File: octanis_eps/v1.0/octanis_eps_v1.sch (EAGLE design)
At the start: 141 parts, among them IC1 OPA2333DGK, Q1 32.768kHz, Q100 BSS123, U1 CSD16327Q3_DQG_8, U10 CSD16327Q3_DQG_8, U100 Value, U11 CSD16327Q3_DQG_8, U2 CSD16327Q3_DQG_8, U3 CSD16327Q3_DQG_8, U4 MSP430G2544, U5 TPS2022D, U6 Value, U7 Value, U8 TPS61232, U9 BQ24650_RVA_16

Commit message: restored old v0.5, renamed v1.0 correctly
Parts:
- removed U100: Value, octanis_eps_v05:TPS630250RNCR
- added Q2: BSC340N08NS3G, transistor-power:BSC340N08NS3G
- added R42: dnp, resistor:R-EU_R0603
- added U12: TPS630250YFFT, texasinstruments:TPS630250YFFT
- added U13: (no value), Seeed-OPL-ic:PMIC-CJ78M05(TO-252)
- added U14: CSD16327Q3_DQG_8, texasinstruments:CSD16327Q3_DQG_8
- added U15: MSP430FR5969, chips:MSP430FR5969
- R35: value 270k -> 100k
- U6, U7: value Value -> TPS630250YFFT; device octanis_eps_v05:TPS630250RNCR -> texasinstruments:TPS630250YFFT
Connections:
- removed net N$30: Q1.1, U4.XIN/P2.6
- removed net N$36: Q1.2, U4.XOUT/P2.7
- removed net N$75: JP2.2, U4.TEST/SBWTCK
- removed net N$93: JP2.1, R19.1, U4.RST/NMI/SBWTDIO
- removed net N$99: C3.1, FERRITE.2, U4.AVCC
- new net AGND: C3.2, U15.AVSS
- new net N$10: C3.1, FERRITE.1, U15.AVCC
- new net N$13: JP2.1, R19.1, U15.RST/SBWTDIO
- new net N$15: JP2.2, U15.TEST/SBWTCK
- new net N$16: Q1.1, U15.LFXOUT
- new net N$17: Q1.2, U15.LFXIN
- new net N$9: R42.1, U$1.MODE
- net +3V3: now also FERRITE.2, U12.FB, U12.VOUT, U12.VOUT_2, U12.VOUT_3, U15.DVCC; no longer FERRITE.1, U4.DVCC, U7.FB, U7.VOUT, U7.VOUT_2, U7.VOUT_3
- net +3V3_2: now also U7.FB, U7.VOUT, U7.VOUT_2, U7.VOUT_3; no longer U100.FB, U100.VOUT, U100.VOUT_2, U100.VOUT_3
- net A_EXT1: now also JP1.7, U15.P4.0/A8; no longer JP1.1, U4.P2.4/TA2/A4/VREF+/VEREF+
- net A_EXT2: now also JP1.5, U15.P4.1/A9; no longer JP1.3, U4.P3.0/UCB0STE/UCA0CLK/A5
- net A_EXT3: now also JP1.3, U15.P4.2/A10; no longer JP1.5, U4.P3.6/A6
- net A_EXT4: now also JP1.1, U15.P4.3/A11; no longer JP1.7, U4.P3.7/A7
- net BAT_OUT: now also U12.EN, U12.VIN, U12.VINA, U12.VIN_2, U12.VIN_3; no longer U100.VIN, U100.VINA, U100.VIN_2, U100.VIN_3, U7.EN
- net EN_12V: now also U15.P3.5/TB0.4; no longer U4.P1.7/TA2/TDO/TDI
- net EN_3V3_1: now also U15.P4.5; no longer U4.P1.4/SMCLK/TCK
- net EN_3V3_2: now also U15.P4.6, U7.EN; no longer U100.EN, U4.P1.5/TA0/TMS
- net EN_3V3_M: now also U15.P4.4/TB0.5; no longer U4.P1.3/TA2
- net EN_5V: now also U15.P3.6/TB0.5; no longer U4.P1.6/TA1/TDI
- net EN_SC: now also U15.P3.4/TB0.3; no longer U4.P2.5/ROSC
- net GND: now also R42.2, U12.GND, U12.PFM_PWM, U12.PGND, U12.PGND_2, U12.PGND_3, U15.DVSS, U15.VSS_QFN, U6.PGND_2, U6.PGND_3, U7.PGND_2, U7.PGND_3; no longer C3.2, U100.GND, U100.PFM_PWM, U100.PGND, U4.AVSS, U4.DVSS
- net I2C_SCL: now also U15.P1.7/TB0.4/UCB0SOMI/UCB0SCL/TA1.0; no longer U4.P3.2/UCB0SOMI/UCB0SCL
- net I2C_SDA: now also U15.P1.6/TB0.3/UCB0SIMO/UCB0SDA/TA0.0; no longer U4.P3.1/UCB0SIMO/UCB0SDA
- net I_IN: now also U15.P1.1/TA0.2/A1/C1; no longer U4.P2.1/TAINCLK/SMCLK/A1
- net I_OUT: now also U15.P1.0/TA0.1/A0/C0; no longer U4.P2.0/ACLK/A0
- net N$1: now also U12.L1, U12.L1_2, U12.L1_3; no longer U7.L1
- net N$11: now also U7.L1, U7.L1_2, U7.L1_3; no longer U100.L1
- net N$12: now also U7.L2, U7.L2_2, U7.L2_3; no longer U100.L2
- net N$3: now also U12.L2, U12.L2_2, U12.L2_3; no longer U7.L2
- net N$6: now also U6.L1_2, U6.L1_3
- net N$7: now also U6.L2_2, U6.L2_3
- net V_BAT: now also U15.P1.3/TA1.2/UCB0STE/A3/C3; no longer U4.P2.3/TA1/A3/VREF−/VEREF-
- net V_SC: now also U15.P1.2/TA1.1/A2/C2; no longer U4.P2.2/TA0/A2
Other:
- note added: "-> R_ILIM = 100k --> switch current limit = 11.7 A"
- moved on the sheet: C10, C104, C3, C4, C7, FERRITE, JP2, Q1, R104, R19, R27

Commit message: now all EPS components are on top side
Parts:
- removed JP1: (no value), Headerlibrary:PINHD-2X4
- removed U13: (no value), Seeed-OPL-ic:PMIC-CJ78M05(TO-252)
- removed U14: CSD16327Q3_DQG_8, texasinstruments:CSD16327Q3_DQG_8
- added C39, C40: 12pF, rcl:C-EUC0603
- added JP7: (no value), adafruit:PINHD-1X6B
- added JP8: (no value), Headerlibrary:PINHD-2X6
- added R43: 1M, rcl:R-EU_R0603
- added RT1, RT3, RT4: 2723, rcl:R-EU_R0603
- added RT2: 8501, rcl:R-EU_R0603
- added RTH: (no value), Headerlibrary:PINHD-1X2
- added U$4: MIC4414, Octanis1_EPS:MIC4414
- Q2: value BSC340N08NS3G -> BSC0901NS
- R41: device rcl:R-EU_R2012 -> rcl:R-EU_R2010
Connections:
- new net A4_EXT: JP8.11, RT3.2, U15.P1.4/TB0.1/UCA0STE/A4/C4
- new net A5_EXT: JP8.9, RT4.2, U15.P1.5/TB0.2/UCA0CLK/A5/C5
- new net AVCC: C3.1, FERRITE.1, RT3.1, RT4.1, U15.AVCC
- new net BAT_11V: C33.1, C34.1, C35.1, L4.1, Q2G$1.S, U$1.EN, U$1.VIN
- new net N$18: JP7.3, U15.P2.1/TB0.0/UCA0RXD/UCA0SOMI
- new net N$28: JP7.4, U15.P2.0/TB0.6/UCA0TXD/UCA0SIMO
- new net N$29: JP7.2, U15.P2.3/TA0.0/UCA1STE/A6
- new net N$30: JP7.1, U15.P2.4/TA1.0/UCA1CLK/A7
- new net N$36: JP7.5, U15.P2.6/TB0.1/UCA1RXD/UCA1SOMI
- new net N$41: JP7.6, U15.P2.5/TB0.0/UCA1TXD/UCA1SIMO
- new net TS: RT1.2, RT2.1, RTH.2, U9.TS
- net AGND: now also C39.1, C40.1, JP8.10, JP8.12, JP8.2, JP8.4, JP8.6, JP8.8, Q1.GND
- net A_EXT1: now also JP8.7; no longer JP1.7
- net A_EXT2: now also JP8.5; no longer JP1.5
- net A_EXT3: now also JP8.3; no longer JP1.3
- net A_EXT4: now also JP8.1; no longer JP1.1
- net BAT_OUT: now also Q2G$1.D, U$4.VDD; no longer C33.1, C34.1, C35.1, L4.1, U$1.VIN
- net EN_12V: now also R43.2, U$4.IN; no longer U$1.EN
- net GND: now also R43.1, RT2.2, RTH.1, U$4.GND; no longer JP1.2, JP1.4, JP1.6, JP1.8, Q1.GND
- net N$10: now also Q2G$1.G, U$4.OUT; no longer C3.1, FERRITE.1, U15.AVCC
- net N$16: now also C39.2
- net N$17: now also C40.2
- net N$72: now also RT1.1
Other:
- note added: "The effective load capacitance, CL,eff can be computed as CIN x COUT / (CIN + COUT), where CIN and COUT are the total capacitance at the LFXIN and LFXOUT terminals, respectively. Cin = 2pF Requires external capacitors at both terminals to meet the effective load capacitance specified by crystal manufacturers. Recommended effective load capacitance values supported are 3.7 pF, 6 pF, 9 pF, and 12.5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"
- moved on the sheet: C23, Q2, R41

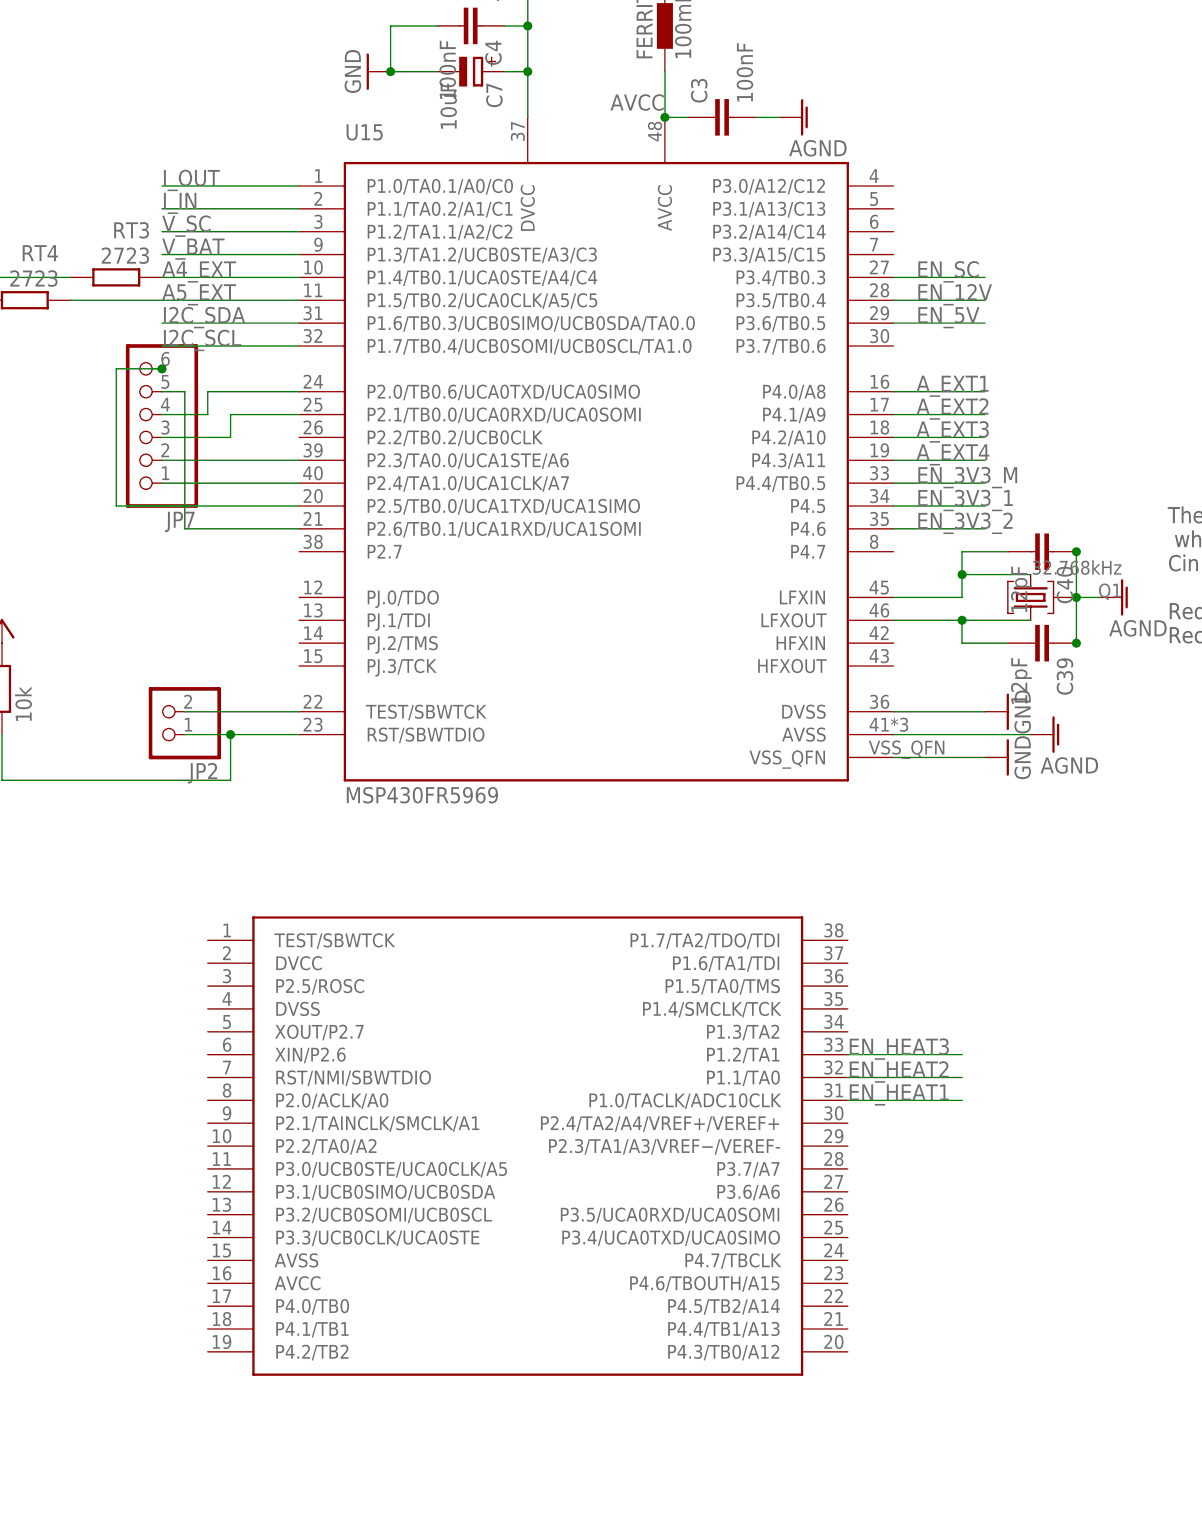
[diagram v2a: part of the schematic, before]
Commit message: finished component placement of new EPS
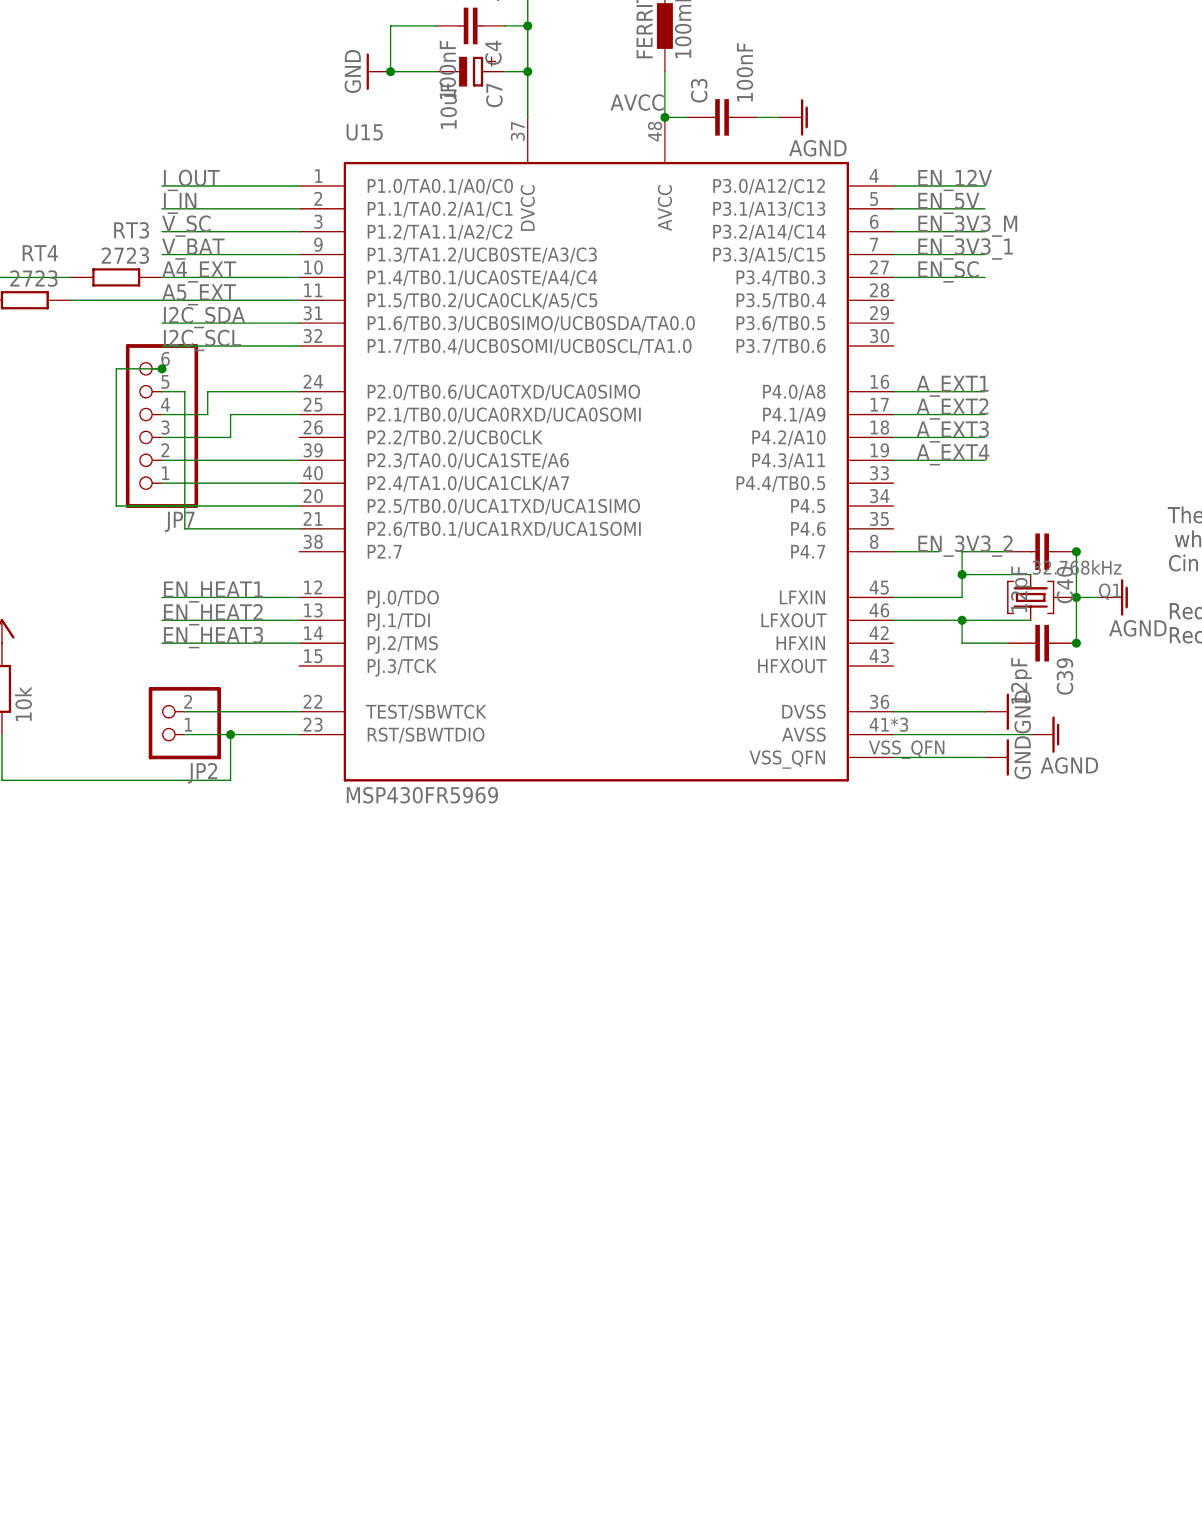
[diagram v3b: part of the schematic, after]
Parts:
- removed U4: MSP430G2544, Octanis1_EPS:MSP430G2544
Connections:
- net EN_12V: now also U15.P3.0/A12/C12; no longer U15.P3.5/TB0.4
- net EN_3V3_1: now also U15.P3.3/A15/C15; no longer U15.P4.5
- net EN_3V3_2: now also U15.P4.7; no longer U15.P4.6
- net EN_3V3_M: now also U15.P3.2/A14/C14; no longer U15.P4.4/TB0.5
- net EN_5V: now also U15.P3.1/A13/C13; no longer U15.P3.6/TB0.5
- net EN_HEAT1: now also U15.PJ.0/TDO; no longer U4.P1.0/TACLK/ADC10CLK
- net EN_HEAT2: now also U15.PJ.1/TDI; no longer U4.P1.1/TA0
- net EN_HEAT3: now also U15.PJ.2/TMS; no longer U4.P1.2/TA1
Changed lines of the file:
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@@
 <part name="U9" library="octanis_eps_v05" deviceset="BQ24650_RVA_16" device=""/>
 <part name="U5" library="Octanis1_EPS" deviceset="TPS2022D" device=""/>
-<part name="U4" library="Octanis1_EPS" deviceset="MSP430G2544" device=""/>
 <part name="C14" library="resistor" deviceset="C-EU" device="C0805" value="10uF"/>
 <part name="C5" library="resistor" deviceset="C-EU" device="C0805" value="22uF"/>
@@
 <instance part="U9" gate="A" x="99.06" y="68.58"/>
 <instance part="U5" gate="G$1" x="419.1" y="175.26"/>
-<instance part="U4" gate="G$1" x="101.6" y="261.62"/>
 <instance part="C14" gate="G$1" x="297.18" y="165.1"/>
 <instance part="C5" gate="G$1" x="365.76" y="165.1"/>
@@
 </segment>
 <segment>
-<pinref part="U4" gate="G$1" pin="P1.0/TACLK/ADC10CLK"/>
-<wire x1="137.16" y1="266.7" x2="149.86" y2="266.7" width="0.1524" layer="91"/>
-<label x="137.16" y="266.7" size="1.778" layer="95"/>
+<pinref part="U15" gate="G$1" pin="PJ.0/TDO"/>
+<wire x1="76.2" y1="322.58" x2="68.58" y2="322.58" width="0.1524" layer="91"/>
+<wire x1="68.58" y1="322.58" x2="60.96" y2="322.58" width="0.1524" layer="91"/>
+<label x="60.96" y="322.58" size="1.778" layer="95"/>
 </segment>
 </net>
@@
 </segment>
 <segment>
-<pinref part="U4" gate="G$1" pin="P1.1/TA0"/>
-<wire x1="137.16" y1="269.24" x2="149.86" y2="269.24" width="0.1524" layer="91"/>
-<label x="137.16" y="269.24" size="1.778" layer="95"/>
+<pinref part="U15" gate="G$1" pin="PJ.1/TDI"/>
+<wire x1="76.2" y1="320.04" x2="60.96" y2="320.04" width="0.1524" layer="91"/>
+<label x="60.96" y="320.04" size="1.778" layer="95"/>
 </segment>
 </net>
@@
 </segment>
 <segment>
-<pinref part="U4" gate="G$1" pin="P1.2/TA1"/>
-<wire x1="137.16" y1="271.78" x2="149.86" y2="271.78" width="0.1524" layer="91"/>
-<label x="137.16" y="271.78" size="1.778" layer="95"/>
+<pinref part="U15" gate="G$1" pin="PJ.2/TMS"/>
+<wire x1="76.2" y1="317.5" x2="60.96" y2="317.5" width="0.1524" layer="91"/>
+<label x="60.96" y="317.5" size="1.778" layer="95"/>
 </segment>
 </net>
@@
 </segment>
 <segment>
-<pinref part="U15" gate="G$1" pin="P4.6"/>
-<wire x1="142.24" y1="330.2" x2="152.4" y2="330.2" width="0.1524" layer="91"/>
-<label x="144.78" y="330.2" size="1.778" layer="95"/>
+<pinref part="U15" gate="G$1" pin="P4.7"/>
+<wire x1="142.24" y1="327.66" x2="147.32" y2="327.66" width="0.1524" layer="91"/>
+<label x="144.78" y="327.66" size="1.778" layer="95"/>
 </segment>
 </net>
@@
 </segment>
 <segment>
-<pinref part="U15" gate="G$1" pin="P3.6/TB0.5"/>
-<wire x1="142.24" y1="353.06" x2="152.4" y2="353.06" width="0.1524" layer="91"/>
-<label x="144.78" y="353.06" size="1.778" layer="95"/>
+<pinref part="U15" gate="G$1" pin="P3.1/A13/C13"/>
+<wire x1="142.24" y1="365.76" x2="152.4" y2="365.76" width="0.1524" layer="91"/>
+<label x="144.78" y="365.76" size="1.778" layer="95"/>
 </segment>
 </net>
 <net name="EN_12V" class="0">
-<segment>
-<pinref part="U15" gate="G$1" pin="P3.5/TB0.4"/>
-<wire x1="142.24" y1="355.6" x2="152.4" y2="355.6" width="0.1524" layer="91"/>
-<label x="144.78" y="355.6" size="1.778" layer="95"/>
-</segment>
 <segment>
 <pinref part="U$4" gate="G$1" pin="IN"/>
@@
 <wire x1="449.58" y1="63.5" x2="441.96" y2="63.5" width="0.1524" layer="91"/>
 <junction x="449.58" y="63.5"/>
+</segment>
+<segment>
+<pinref part="U15" gate="G$1" pin="P3.0/A12/C12"/>
+<wire x1="142.24" y1="368.3" x2="152.4" y2="368.3" width="0.1524" layer="91"/>
+<label x="144.78" y="368.3" size="1.778" layer="95"/>
 </segment>
 </net>
@@
 </segment>
 <segment>
-<pinref part="U15" gate="G$1" pin="P4.4/TB0.5"/>
-<wire x1="142.24" y1="335.28" x2="152.4" y2="335.28" width="0.1524" layer="91"/>
-<label x="144.78" y="335.28" size="1.778" layer="95"/>
+<pinref part="U15" gate="G$1" pin="P3.2/A14/C14"/>
+<wire x1="142.24" y1="363.22" x2="152.4" y2="363.22" width="0.1524" layer="91"/>
+<label x="144.78" y="363.22" size="1.778" layer="95"/>
 </segment>
 </net>
@@
 </segment>
 <segment>
-<pinref part="U15" gate="G$1" pin="P4.5"/>
-<wire x1="142.24" y1="332.74" x2="149.86" y2="332.74" width="0.1524" layer="91"/>
-<wire x1="149.86" y1="332.74" x2="152.4" y2="332.74" width="0.1524" layer="91"/>
-<label x="144.78" y="332.74" size="1.778" layer="95"/>
-</segment>
-</net>
+<pinref part="U15" gate="G$1" pin="P3.3/A15/C15"/>
+<wire x1="142.24" y1="360.68" x2="152.4" y2="360.68" width="0.1524" layer="91"/>
+<label x="144.78" y="360.68" size="1.778" layer="95"/>
+</segment>
+</net>
